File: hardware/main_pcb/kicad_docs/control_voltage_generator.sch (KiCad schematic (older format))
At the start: 22 parts, among them J5 extern_resolution_CV, J6 extern_sample_rate_CV, U2 MCP6002-xP

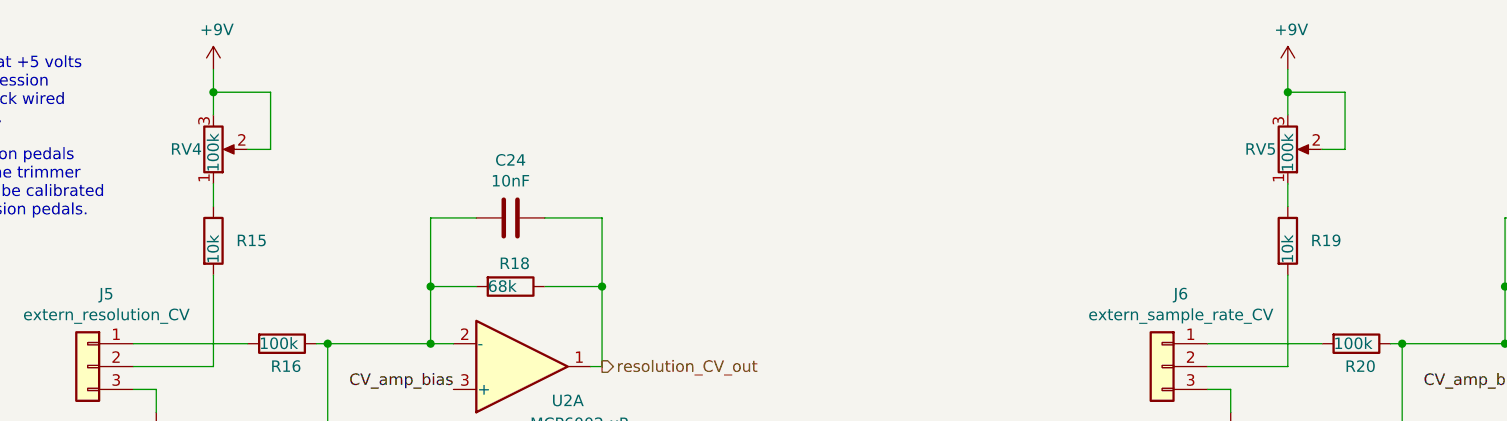
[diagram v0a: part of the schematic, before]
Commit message: switch trimpot rotation
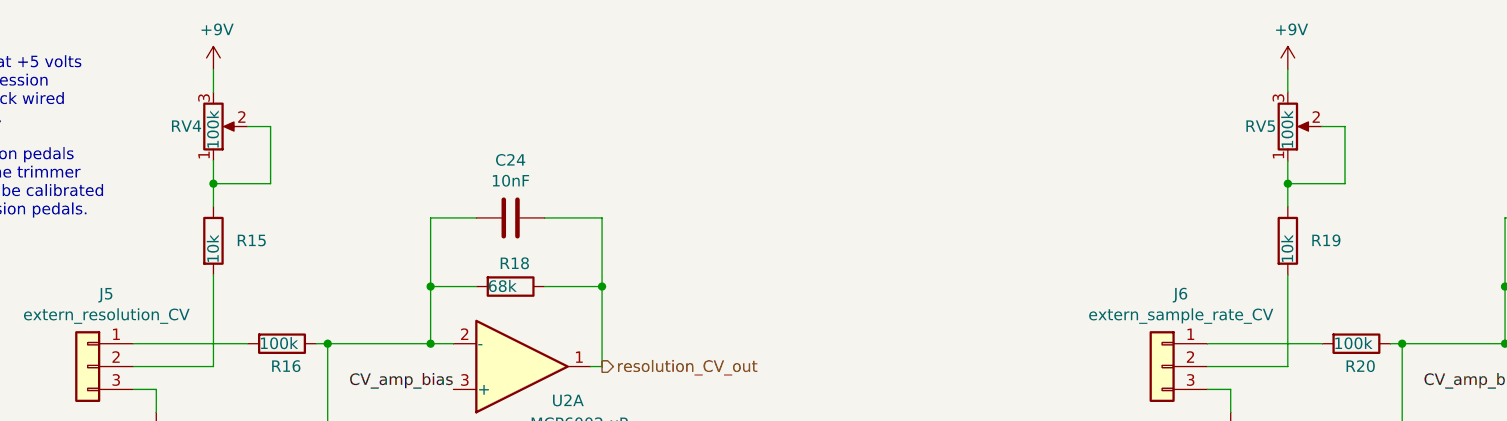
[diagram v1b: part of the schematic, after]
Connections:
- net +9V: no longer RV4.2, RV5.2
- net at R15.1, RV4.1: now also RV4.2
- net at R19.1, RV5.1: now also RV5.2
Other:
- moved on the sheet: RV4, RV5
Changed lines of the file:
@@
 L Device:R_POT RV4
 U 1 1 5F39ECFC
-P 3100 2200
-F 0 "RV4" H 3050 2200 50  0000 R CNN
-F 1 "100k" V 3100 2300 50  0000 R CNN
-F 2 "Potentiometer_THT:Potentiometer_Bourns_3296W_Vertical" H 3100 2200 50  0001 C CNN
-F 3 "~" H 3100 2200 50  0001 C CNN
-	1    3100 2200
+P 3100 2100
+F 0 "RV4" H 3050 2100 50  0000 R CNN
+F 1 "100k" V 3100 2200 50  0000 R CNN
+F 2 "Potentiometer_THT:Potentiometer_Bourns_3296W_Vertical" H 3100 2100 50  0001 C CNN
+F 3 "~" H 3100 2100 50  0001 C CNN
+	1    3100 2100
 	1    0    0    1
 $EndComp
 Wire Wire Line
-	3350 2200 3250 2200
+	3350 2100 3250 2100
 Wire Wire Line
-	3100 1850 3100 1950
-Wire Wire Line
-	3100 2350 3100 2450
-Wire Wire Line
-	3350 2200 3350 1950
-Wire Wire Line
-	3350 1950 3100 1950
-Connection ~ 3100 1950
-Wire Wire Line
-	3100 1950 3100 2050
+	3100 2250 3100 2350
 Wire Wire Line
 	7800 3150 7800 2750
@@
 	1    0    0    -1
 $EndComp
+Wire Wire Line
+	8050 2100 7950 2100
+Wire Wire Line
+	7800 2250 7800 2350
+Wire Wire Line
+	3100 1850 3100 1950
+Wire Wire Line
+	3100 2350 3350 2350
+Wire Wire Line
+	3350 2350 3350 2100
+Connection ~ 3100 2350
+Wire Wire Line
+	3100 2350 3100 2450
 $Comp
 L Device:R_POT RV5
 U 1 1 5F3B36D5
-P 7800 2200
-F 0 "RV5" H 7750 2200 50  0000 R CNN
-F 1 "100k" V 7800 2300 50  0000 R CNN
-F 2 "Potentiometer_THT:Potentiometer_Bourns_3296W_Vertical" H 7800 2200 50  0001 C CNN
-F 3 "~" H 7800 2200 50  0001 C CNN
-	1    7800 2200
+P 7800 2100
+F 0 "RV5" H 7750 2100 50  0000 R CNN
+F 1 "100k" V 7800 2200 50  0000 R CNN
+F 2 "Potentiometer_THT:Potentiometer_Bourns_3296W_Vertical" H 7800 2100 50  0001 C CNN
+F 3 "~" H 7800 2100 50  0001 C CNN
+	1    7800 2100
 	1    0    0    1
 $EndComp
 Wire Wire Line
-	8050 2200 7950 2200
-Wire Wire Line
 	7800 1850 7800 1950
 Wire Wire Line
+	7800 2350 8050 2350
+Wire Wire Line
+	8050 2350 8050 2100
+Connection ~ 7800 2350
+Wire Wire Line
 	7800 2350 7800 2450
-Wire Wire Line
-	8050 2200 8050 1950
-Wire Wire Line
-	8050 1950 7800 1950
-Connection ~ 7800 1950
-Wire Wire Line
-	7800 1950 7800 2050
 $EndSCHEMATC

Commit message: rev 1.1, fix silkscreen, flip trimpots, adjust hpf
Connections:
- net +9V: now also RV4.1, RV5.1; no longer RV4.3, RV5.3
- net at R15.1, RV4.2: now also RV4.3; no longer RV4.1
- net at R19.1, RV5.2: now also RV5.3; no longer RV5.1
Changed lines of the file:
@@
 F 3 "~" H 3100 2100 50  0001 C CNN
 	1    3100 2100
-	1    0    0    1
+	1    0    0    -1
 $EndComp
 Wire Wire Line
@@
 F 3 "~" H 7800 2100 50  0001 C CNN
 	1    7800 2100
-	1    0    0    1
+	1    0    0    -1
 $EndComp
 Wire Wire Line

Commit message: flip trimpots again, hopefully right this time
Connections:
- net +9V: now also RV4.3, RV5.3; no longer RV4.1, RV5.1
- net at R15.1, RV4.2: now also RV4.1; no longer RV4.3
- net at R19.1, RV5.2: now also RV5.1; no longer RV5.3
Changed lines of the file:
@@
-	1    0    0    -1
-$EndComp
-$Comp
-L Device:R_POT RV4
-U 1 1 5F39ECFC
-P 3100 2100
-F 0 "RV4" H 3050 2100 50  0000 R CNN
-F 1 "100k" V 3100 2200 50  0000 R CNN
-F 2 "Potentiometer_THT:Potentiometer_Bourns_3296W_Vertical" H 3100 2100 50  0001 C CNN
-F 3 "~" H 3100 2100 50  0001 C CNN
-	1    3100 2100
 	1    0    0    -1
 $EndComp
 Wire Wire Line
 	3350 2100 3250 2100
-Wire Wire Line
-	3100 2250 3100 2350
 Wire Wire Line
 	7800 3150 7800 2750
@@
 F 3 "~" H 7800 2100 50  0001 C CNN
 	1    7800 2100
-	1    0    0    -1
+	1    0    0    1
 $EndComp
 Wire Wire Line
@@
 Wire Wire Line
 	7800 2350 7800 2450
+Wire Wire Line
+	3100 2250 3100 2350
+$Comp
+L Device:R_POT RV4
+U 1 1 5F39ECFC
+P 3100 2100
+F 0 "RV4" H 3050 2100 50  0000 R CNN
+F 1 "100k" V 3100 2200 50  0000 R CNN
+F 2 "Potentiometer_THT:Potentiometer_Bourns_3296W_Vertical" H 3100 2100 50  0001 C CNN
+F 3 "~" H 3100 2100 50  0001 C CNN
+	1    3100 2100
+	1    0    0    1
+$EndComp
 $EndSCHEMATC
